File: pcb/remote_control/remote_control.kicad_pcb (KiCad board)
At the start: 2 copper layers, 35 parts, among them J1 Conn_01x04, SW1 SW_Push, SW2 SW_DPDT_x2, SW3 SW_Push, U1 AMS1117-3.3, U2 AMS1117-5.0, U3 STM32F031C6Tx, U4 Rocker, U5 Rocker, Y1 8M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

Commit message: Layout remote_control board.
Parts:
- added Lora1: Conn_01x07, Connector_PinSocket_2.54mm:PinSocket_1x07_P2.54mm_Vertical, F.Cu at (141.2, 37.6)
- moved BT1 179.3 mm to (333.5, 90.0)
- moved C8 161.9 mm to (261.0, 38.0)
- moved C5 160.6 mm to (280.6, 42.0)
- moved Y2 155.8 mm to (247.2, 38.1)
- moved C11 152.6 mm to (271.3, 54.3)
- moved C2 145.5 mm to (280.6, 44.5)
- moved C13 144.5 mm to (257.0, 38.0)
- moved R3 143.6 mm to (253.0, 40.5)
- moved C14 137.8 mm to (253.0, 38.0)
- moved C7 127.5 mm to (253.0, 45.5)
- moved C9 125.3 mm to (253.0, 43.0)
- moved Y1 123.0 mm to (224.1, 50.9)
- moved U1 122.1 mm to (249.3, 54.0)
- moved SW1 116.0 mm to (207.8, 59.9)
- moved R2 113.3 mm to (226.4, 68.4)
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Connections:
- U3 pad 33: /PA12 -> /AUX
- U3 pad 42: /PB6 -> /USART1_TX
- U3 pad 43: /PB7 -> /USART1_RX
- U3 pad 45: /PB8 -> /MD1
- U3 pad 46: /PB9 -> /MD0
- U4 pad 1: Net-(U4-Pad1) -> /PA0
- U4 pad 2: Net-(U4-Pad2) -> /PA1
- U4 pad 3: Net-(U4-Pad3) -> /PF6
- U4 pad 5: Net-(U4-Pad5) -> +3.3VA
- U5 pad 1: Net-(U5-Pad1) -> /PA2
- U5 pad 2: Net-(U5-Pad2) -> /PA3
- U5 pad 3: Net-(U5-Pad3) -> /PF7
- U5 pad 5: Net-(U5-Pad5) -> +3.3VA
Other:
- board outline added: 99.1 x 99.1 mm

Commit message: Update remote_control board.
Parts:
- removed BT1: Battery, Battery:BatteryHolder_Eagle_12BH611-GR
- removed C10, C11, C13, C4, C9: 100nF, Capacitor_SMD:C_0603_1608Metric
- removed C12: 4.7uF, Capacitor_SMD:C_0805_2012Metric
- removed C14: 1uF, Capacitor_SMD:C_0603_1608Metric
- removed C15: 10nF, Capacitor_SMD:C_0603_1608Metric
- removed C3: 10uF, Capacitor_SMD:C_0805_2012Metric
- removed C5, C6: 20pF, Capacitor_SMD:C_0603_1608Metric
- removed C7, C8: 10pF, Capacitor_SMD:C_0603_1608Metric
- removed D2: LED, LED_SMD:LED_0805_2012Metric
- removed L1: 10uH, Inductor_SMD:L_0805_2012Metric
- removed R2: 510R, Resistor_SMD:R_0603_1608Metric
- removed R3: 390, Resistor_SMD:R_0603_1608Metric
- removed R4: 10K, Resistor_SMD:R_0603_1608Metric
- removed R5: 0R, Resistor_SMD:R_0805_2012Metric
- removed SW2: SW_DPDT_x2, Connector_PinHeader_2.54mm:PinHeader_1x03_P2.54mm_Vertical
- removed SW3: SW_Push, Button_Switch_SMD:SW_SPST_CK_RS282G05A3
- removed U2: AMS1117-5.0, Package_TO_SOT_SMD:SOT-223-3_TabPin2
- removed U3: STM32F031C6Tx, Package_QFP:LQFP-48_7x7mm_P0.5mm
- removed Y1: 8M, Crystal:Crystal_HC49-4H_Vertical
- removed Y2: 32.768, Crystal:Crystal_C38-LF_D3.0mm_L8.0mm_Horizontal
- added J2: Conn_02x20_Odd_Even, Connector_PinSocket_2.54mm:PinSocket_2x20_P2.54mm_Horizontal, F.Cu at (110.5, 64.8)
- J1: value Conn_01x04 -> Conn_01x02; footprint Connector_PinHeader_2.54mm:PinHeader_1x04_P2.54mm_Vertical -> Connector_PinSocket_2.54mm:PinSocket_1x02_P2.54mm_Vertical
- U1: value AMS1117-3.3 -> AMS1117-5.0
- moved C2 157.4 mm to (123.7, 55.6)
- moved U1 112.9 mm to (136.5, 50.2)
- moved R1 103.6 mm to (123.7, 52.6)
- moved C1 89.4 mm to (147.3, 55.9)
- moved SW1 88.5 mm to (120.7, 44.5)
- moved J1 86.1 mm to (90.2, 68.6)
- moved D1 80.6 mm to (143.7, 47.6)
- moved U5 76.5 mm to (163.8, 41.9), turned to 0 degrees
- moved U4 70.8 mm to (94.0, 41.9), turned to 0 degrees
- moved Lora1 16.8 mm to (124.5, 37.6), turned to 90 degrees
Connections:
- C1 pad 1: +3V3 -> +5V
- C2 pad 1: +3V3 -> +5V
- J1 pad 1: GNDD -> VCC
- J1 pad 2: /SYS_SWCL -> GNDD
- Lora1 pad 3: /AUX -> /PB14
- Lora1 pad 4: /USART1_RX -> /PB7
- Lora1 pad 5: /USART1_TX -> /PB6
- Lora1 pad 6: /MD1 -> /PB13
- Lora1 pad 7: /MD0 -> /PB12
- R1 pad 2: +3V3 -> +5V
- SW1 pad 1: Net-(BT1-Pad1) -> VCC
- SW1 pad 2: VCC -> Net-(SW1-Pad2)
- U1 pad 2: +3V3 -> +5V
- U1 pad 3: VCC -> Net-(SW1-Pad2)
- U4 pad 3: /PF6 -> /PB15
- U5 pad 3: /PF7 -> /PA12

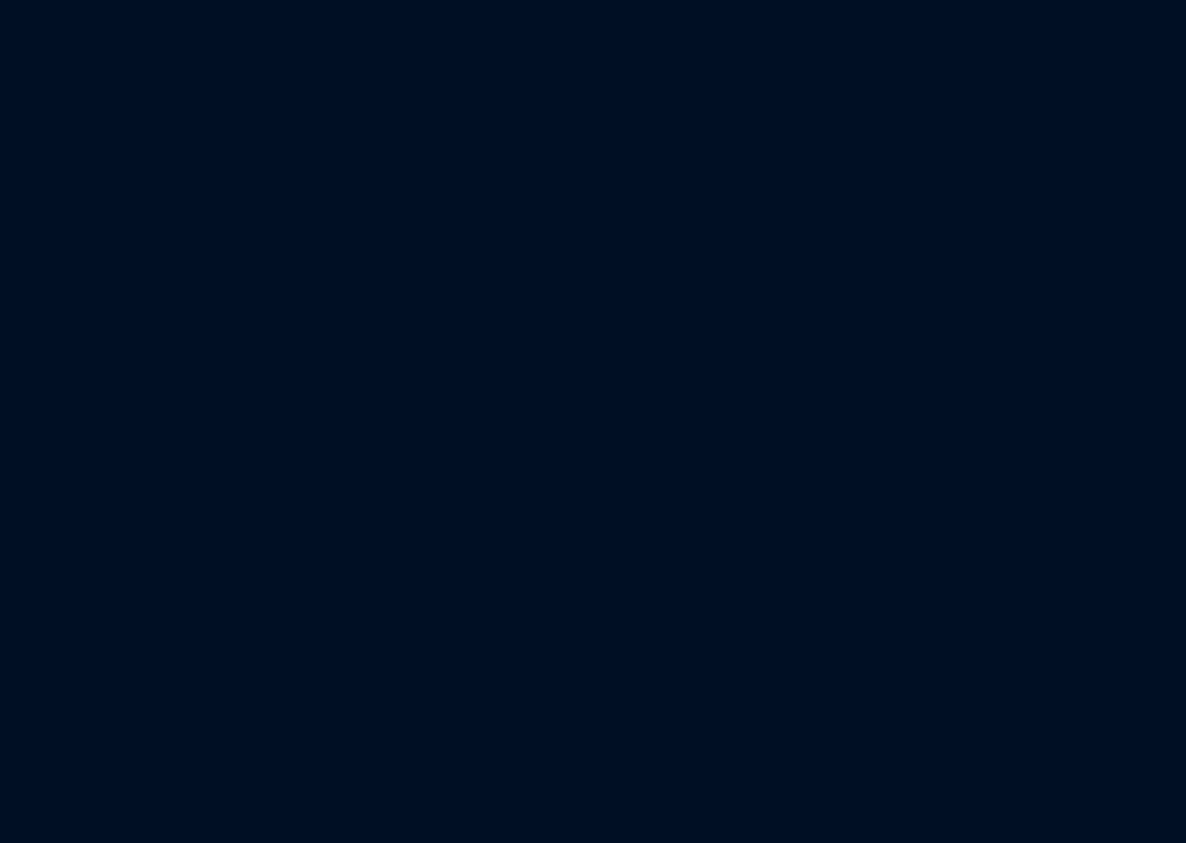
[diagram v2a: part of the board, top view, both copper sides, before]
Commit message: Update footprint and symbol for remote_control board.
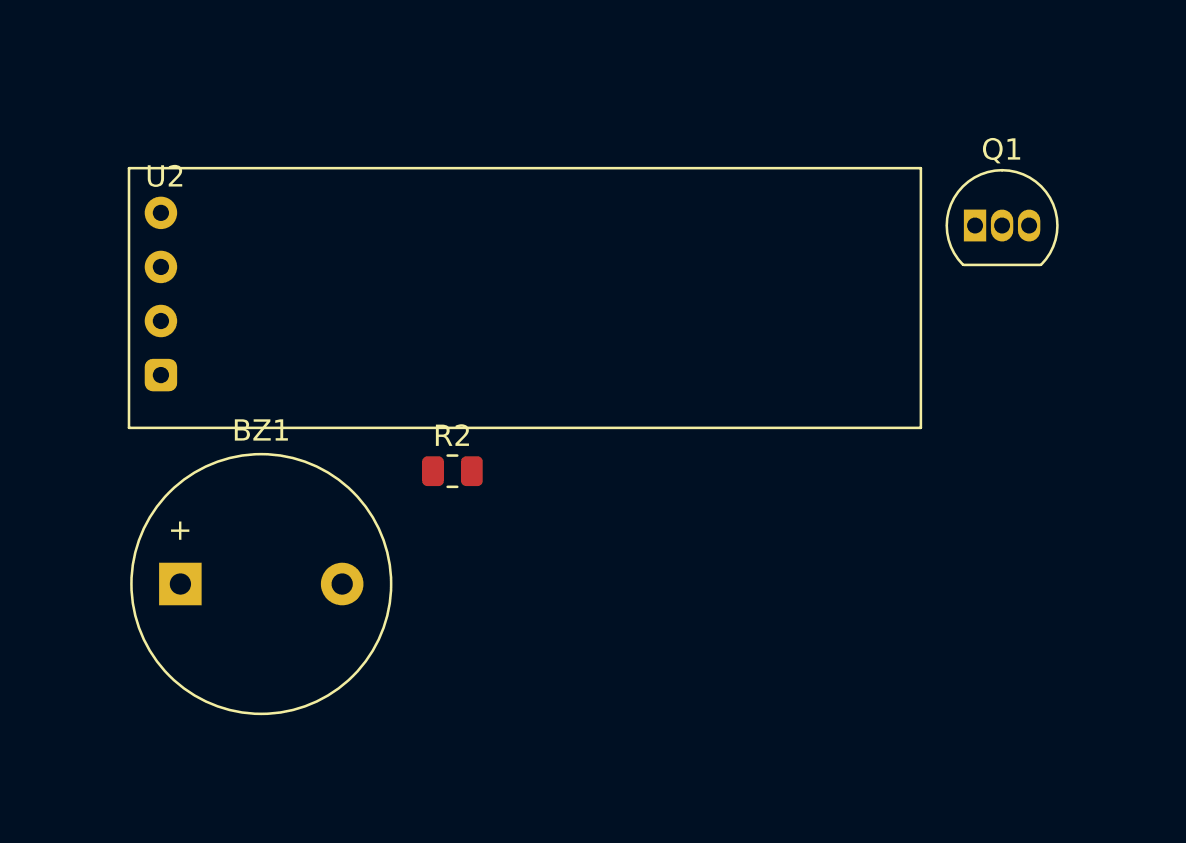
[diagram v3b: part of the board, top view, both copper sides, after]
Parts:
- added BZ1: Buzzer, Buzzer_Beeper:Buzzer_12x9.5RM7.6, F.Cu at (116.3, 105.7)
- added Q1: S8050, Package_TO_SOT_THT:TO-92_Inline, F.Cu at (153.7, 88.8)
- added R2: 510R, Resistor_SMD:R_0805_2012Metric, F.Cu at (129.1, 100.4)
- added U2: OLED0.91'', Footprint:OLED_0.91, F.Cu at (115.4, 88.2)

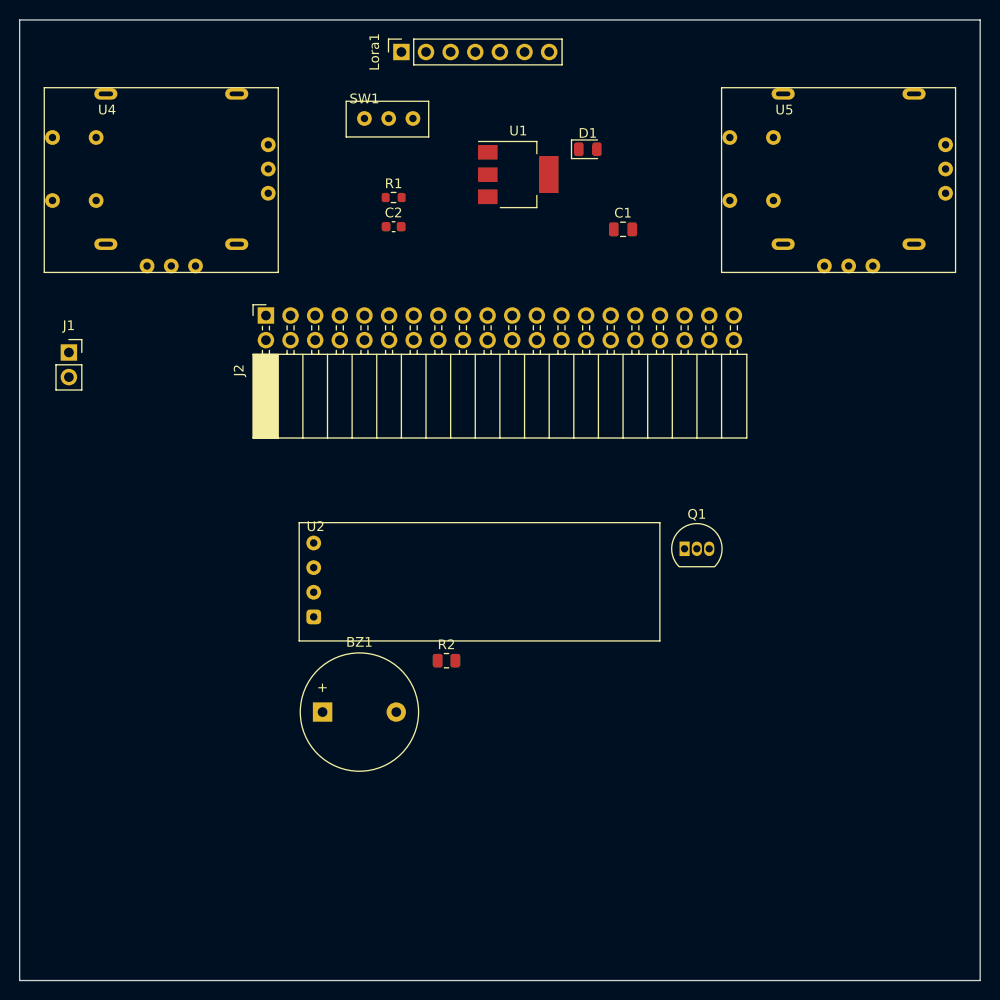
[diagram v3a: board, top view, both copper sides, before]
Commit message: Complete layout for remote_control board.
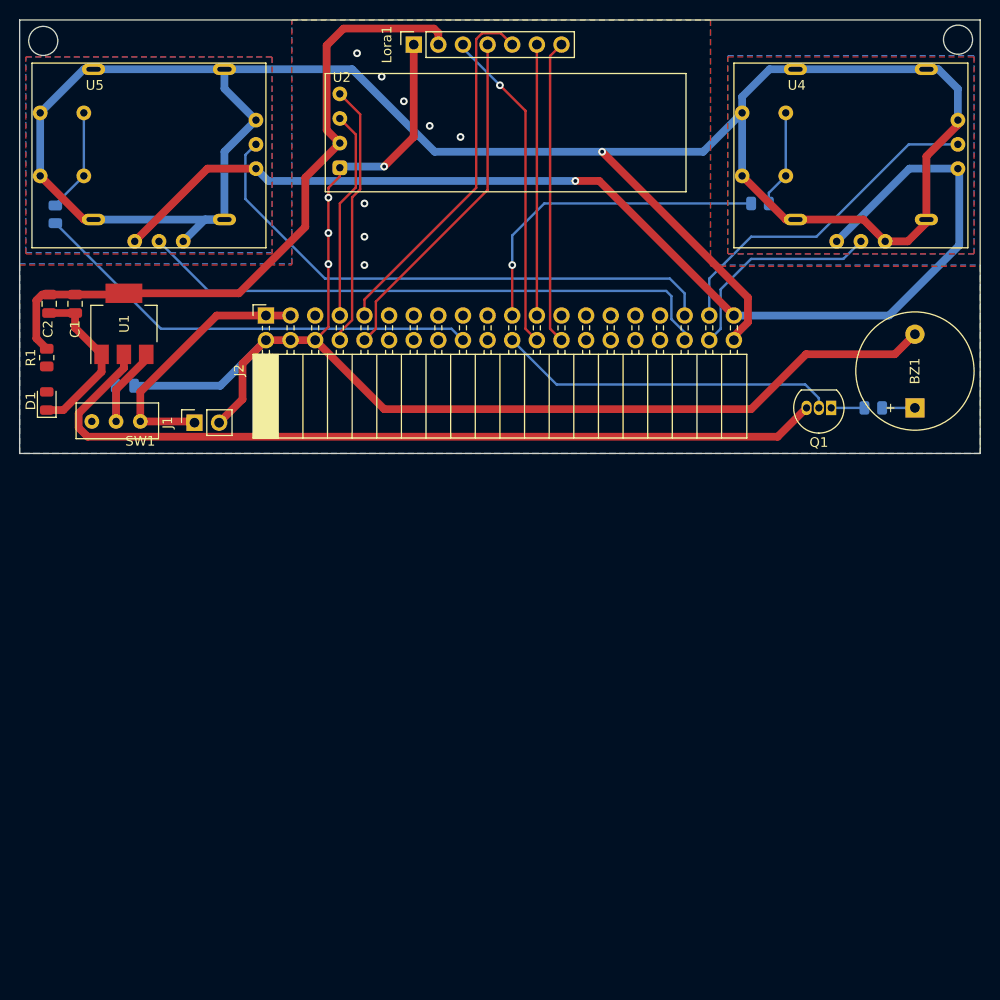
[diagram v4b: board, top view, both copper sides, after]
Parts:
- added C3: 10uF, Capacitor_SMD:C_0805_2012Metric, B.Cu at (95.9, 72.0)
- added R3: 510R, Resistor_SMD:R_0805_2012Metric, B.Cu at (88.8, 54.3)
- added R4: 510R, Resistor_SMD:R_0805_2012Metric, B.Cu at (161.4, 53.2)
- C2: footprint Capacitor_SMD:C_0603_1608Metric -> Capacitor_SMD:C_0805_2012Metric
- R1: footprint Resistor_SMD:R_0603_1608Metric -> Resistor_SMD:R_0805_2012Metric
- R2: moved to B.Cu
- moved U5 71.2 mm to (92.7, 39.4)
- moved U4 71.2 mm to (165.1, 39.4)
- moved BZ1 68.7 mm to (177.4, 74.3), turned to 90 degrees
- moved D1 61.5 mm to (87.9, 73.6), turned to 90 degrees
- moved C1 57.0 mm to (90.8, 63.6), turned to 270 degrees
- moved R2 51.2 mm to (173.1, 74.3), turned to 180 degrees
- moved U2 46.4 mm to (118.1, 41.9)
- moved U1 43.5 mm to (95.8, 65.6), turned to 90 degrees
- moved R1 39.4 mm to (87.9, 69.1), turned to 90 degrees
- moved SW1 38.9 mm to (97.5, 75.7), turned to 180 degrees
- moved C2 36.4 mm to (88.1, 63.6), turned to 270 degrees
- moved Q1 21.0 mm to (168.8, 74.3), turned to 180 degrees
- moved J1 14.8 mm to (103.1, 75.8), turned to 90 degrees
- moved Lora1 1.48 mm to (125.7, 36.8)
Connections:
- U4 pad 3: /PB15 -> Net-(R4-Pad2)
- U5 pad 3: /PA12 -> Net-(R3-Pad2)
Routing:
- net GNDA: track 0.00 -> 226.6 mm, vias 0 -> 1
- net +5V: track 0.00 -> 156.9 mm
- net GNDD: track 0.00 -> 153.6 mm, vias 0 -> 12
- net +3.3VA: track 0.00 -> 121.0 mm, vias 0 -> 1
- net /PA3: track 0.00 -> 60.3 mm
- net /PA2: track 0.00 -> 57.7 mm
- net /PA12: track 0.00 -> 47.0 mm
- net /PB6: track 0.00 -> 37.7 mm
- net /PB7: track 0.00 -> 35.7 mm
- net /PA0: track 0.00 -> 35.2 mm
- net /PA8: track 0.00 -> 35.1 mm
- net /PB15: track 0.00 -> 34.3 mm, vias 0 -> 1
- net /PB14: track 0.00 -> 33.6 mm, vias 0 -> 1
- net /PB12: track 0.00 -> 31.5 mm
- net /PB13: track 0.00 -> 27.9 mm
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- added copper zone on B.Cu, net GNDA
- added copper zone on F.Cu, net GNDA
- added copper zone on B.Cu, net GNDD
- added copper zone on F.Cu, net GNDD
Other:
- board size 99.1 x 99.1 mm -> 99.1 x 44.7 mm
